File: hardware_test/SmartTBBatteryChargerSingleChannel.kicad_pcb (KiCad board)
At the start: 2 copper layers, 100 x 100 mm, 151 parts, among them J1 XT60_MALE, J2 XT60_MALE, J3 XT60_MALE, J7 Conn_SWD, J8 Conn_01x02, Q1 BSC070N10NS5, Q2 BSC070N10NS5, Q3 BSC070N10NS5, U1 RY8411, U10 INA240A1PW, U2 RS3236, U3 RY8411, U4 STM32G474RBTx, U5 INA240A1PW, U6 UCC27517, U7 UCC27517, U8 INA240A1PW, U9 UCC27517, Y1 Crystal_GND24

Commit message: Test Hardware schematic done
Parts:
- removed C51, C52, C61: 100u, Capacitor_THT:CP_Radial_D6.3mm_P2.50mm
- removed C53, C56, C57, C58, C60: 100n, Capacitor_SMD:C_0603_1608Metric
- removed C54, C55, C59: 10u, Capacitor_SMD:C_1206_3216Metric
- removed D16: LED_RED, LED_SMD:LED_0603_1608Metric
- removed D7: K34, Diode_SMD:D_SOD-123F
- removed D8: SB1045, Diode_SMD:D_PowerDI-5
- removed F3: 8A, Fuse:Fuse_1206_3216Metric
- removed J3: XT60_MALE, Connector_AMASS:AMASS_XT60-M_1x02_P7.20mm_Vertical
- removed L5: 47u, Inductor_SMD:L_Coilcraft_MSS1260-XXX
- removed Q3: BSC070N10NS5, Package_TO_SOT_SMD:TDSON-8-1
- removed R18: 10k, Resistor_SMD:R_0603_1608Metric
- removed R19: 90k, Resistor_SMD:R_0603_1608Metric
- removed R20: 4m, Resistor_SMD:R_Shunt_Vishay_WSK2512_6332Metric_T1.19mm
- removed R38: 240k, Resistor_SMD:R_0603_1608Metric
- removed U10: INA240A1PW, Package_SO:TSSOP-8_4.4x3mm_P0.65mm
- removed U9: UCC27517, Package_TO_SOT_SMD:SOT-23-5
- C21: value 100u 6.3V -> C_Polarized; footprint Capacitor_SMD:C_1206_3216Metric -> Capacitor_THT:CP_Radial_D6.3mm_P2.50mm
- C41: value 100u -> 100n; footprint Capacitor_THT:CP_Radial_D6.3mm_P2.50mm -> Capacitor_SMD:C_0603_1608Metric; moved to B.Cu
- C42: value 100n -> 100u; footprint Capacitor_SMD:C_0603_1608Metric -> Capacitor_THT:CP_Radial_D6.3mm_P2.50mm; moved to F.Cu
- C43: value 10u -> 100n; footprint Capacitor_SMD:C_1206_3216Metric -> Capacitor_SMD:C_0603_1608Metric
- C44: value 10u -> 100n; footprint Capacitor_SMD:C_1206_3216Metric -> Capacitor_SMD:C_0603_1608Metric; moved to F.Cu
- C45: value 100n -> 10u; footprint Capacitor_SMD:C_0603_1608Metric -> Capacitor_SMD:C_1206_3216Metric
- C46: value 100n -> 10u; footprint Capacitor_SMD:C_0603_1608Metric -> Capacitor_SMD:C_1206_3216Metric; moved to B.Cu
- C47: value 100n -> 10u; footprint Capacitor_SMD:C_0603_1608Metric -> Capacitor_SMD:C_1206_3216Metric; moved to F.Cu
- C48: value 10u -> 100u; footprint Capacitor_SMD:C_1206_3216Metric -> Capacitor_THT:CP_Radial_D6.3mm_P2.50mm
- C49: moved to B.Cu
- C50: value 100u -> 100n; footprint Capacitor_THT:CP_Radial_D6.3mm_P2.50mm -> Capacitor_SMD:C_0603_1608Metric
- D5: value K34 -> SB1045; footprint Diode_SMD:D_SOD-123F -> Diode_SMD:D_PowerDI-5
- D6: value SB1045 -> K34; footprint Diode_SMD:D_PowerDI-5 -> Diode_SMD:D_SOD-123F
- R11: value 1R -> 33R; moved to F.Cu
- R12: value 33R -> 4m; footprint Resistor_SMD:R_0603_1608Metric -> Resistor_SMD:R_Shunt_Vishay_WSK2512_6332Metric_T1.19mm; moved to B.Cu
- R13: value 10k -> 1R; moved to B.Cu
- R14: value 90k -> 10k
- R15: value 4m -> 90k; footprint Resistor_SMD:R_Shunt_Vishay_WSK2512_6332Metric_T1.19mm -> Resistor_SMD:R_0603_1608Metric; moved to F.Cu
- R16: value 1R -> 33r; moved to F.Cu
- R17: value 33R -> 33r
- U7: value UCC27517 -> INA240A1PW; footprint Package_TO_SOT_SMD:SOT-23-5 -> Package_SO:TSSOP-8_4.4x3mm_P0.65mm
- U8: value INA240A1PW -> UCC27517; footprint Package_SO:TSSOP-8_4.4x3mm_P0.65mm -> Package_TO_SOT_SMD:SOT-23-5
- moved R17 300.4 mm to (111.2, 155.0)
- moved R16 280.3 mm to (111.2, 152.5), turned to 0 degrees
- moved C44 34.4 mm to (400.4, 42.7), turned to 0 degrees
- moved C46 33.3 mm to (367.0, 51.0), turned to 180 degrees
- moved R13 24.7 mm to (381.2, 57.0), turned to -90 degrees
- moved C50 24.2 mm to (400.4, 45.2)
- moved R11 21.2 mm to (400.4, 47.7), turned to 0 degrees
- moved U7 20.9 mm to (369.8, 42.5)
- moved U8 20.5 mm to (384.2, 57.2)
- moved C45 20.0 mm to (365.8, 54.8), turned to -90 degrees
- moved R15 18.9 mm to (400.4, 52.8)
- moved R12 17.0 mm to (383.8, 43.0)
- moved C21 15.7 mm to (104.0, 155.2)
- moved C49 15.4 mm to (386.3, 54.5)
- moved C47 12.3 mm to (382.2, 44.0), turned to -90 degrees
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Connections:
- C41 pad 1: VPP -> +3.3V
- C44 pad 1: VPP -> GND
- C44 pad 2: GND -> ISENSE_CH2
- C45 pad 1: +10V -> VPP
- C46 pad 1: GND -> VPP
- C46 pad 2: ISENSE_CH2 -> GND
- C47 pad 1: +3.3V -> VPP
- C47 pad 2: GND -> Net-(C47-Pad2)
- C48 pad 2: Net-(C48-Pad2) -> Net-(C47-Pad2)
- C49 pad 1: GND -> +10V
- C49 pad 2: VSENSE_CH2 -> GND
- C50 pad 1: VPP -> GND
- C50 pad 2: Net-(C48-Pad2) -> VSENSE_CH2
- D5 pad 1: Net-(D5-K) -> VPP
- D6 pad 1: VPP -> Net-(D6-K)
- F2 pad 2: Net-(C48-Pad2) -> Net-(C47-Pad2)
- L4 pad 1: Net-(D6-A) -> Net-(D5-A)
- L4 pad 2: Net-(C48-Pad2) -> Net-(C47-Pad2)
- Q2 pad 4: Net-(D5-A) -> Net-(D6-A)
- Q2 pad 5: Net-(D6-A) -> Net-(D5-A)
- R11 pad 1: Net-(D5-K) -> ISENSE_CH2
- R11 pad 2: Net-(D5-A) -> Net-(R11-Pad2)
- R12 pad 1: ISENSE_CH2 -> VPP
- R12 pad 2: Net-(R12-Pad2) -> Net-(U7--)
- R13 pad 1: GND -> Net-(D6-K)
- R13 pad 2: VSENSE_CH2 -> Net-(D6-A)
- R14 pad 1: VSENSE_CH2 -> GND
- R14 pad 2: Net-(C48-Pad2) -> VSENSE_CH2
- R15 pad 1: VPP -> VSENSE_CH2
- R15 pad 2: Net-(U8--) -> Net-(C47-Pad2)
- R16 pad 1: Net-(D7-K) -> DRV_CH1
- R16 pad 2: Net-(D7-A) -> Net-(U4-PA8)
- R17 pad 1: ISENSE_CH3 -> DRV_CH2
- R17 pad 2: Net-(R17-Pad2) -> Net-(U4-PA10)
- U4 pad 15: Net-(U4-VSS-Pad15) -> GND
- U4 pad 27: unconnected-(U4-VSSA-Pad27) -> GND
- U4 pad 31: Net-(U4-VSS-Pad15) -> GND
- U4 pad 33: unconnected-(U4-PB11-Pad33) -> VSENSE_CH1
- U4 pad 35: unconnected-(U4-PB13-Pad35) -> VSENSE_CH2
- U4 pad 42: unconnected-(U4-PA8-Pad42) -> Net-(U4-PA8)
- U4 pad 44: unconnected-(U4-PA10-Pad44) -> Net-(U4-PA10)
- U4 pad 47: Net-(U4-VSS-Pad15) -> GND
- U4 pad 63: Net-(U4-VSS-Pad15) -> GND
- U4 pad 8: unconnected-(U4-PC0-Pad8) -> ISENSE_CH1
- U4 pad 9: unconnected-(U4-PC1-Pad9) -> ISENSE_CH2
- U7 pad 1: +10V -> GND
- U7 pad 2: GND -> Net-(U7-+)
- U7 pad 3: DRV_CH2 -> Net-(U7--)
- U7 pad 5: Net-(D5-K) -> +3.3V
- U8 pad 1: GND -> +10V
- U8 pad 2: Net-(U8-+) -> GND
- U8 pad 3: Net-(U8--) -> DRV_CH2
- U8 pad 5: +3.3V -> Net-(D6-K)

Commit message: Progress on hardware_test PCB
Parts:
- removed C24: 100n, Capacitor_SMD:C_0603_1608Metric
- removed Y1: Crystal_GND24, Crystal:Crystal_SMD_3225-4Pin_3.2x2.5mm
- added C51: 100n, Capacitor_SMD:C_0603_1608Metric, F.Cu at (227.1, 137.3)
- added C52: 100n, Capacitor_SMD:C_0603_1608Metric, F.Cu at (208.0, 131.6)
- added C53: 100n, Capacitor_SMD:C_0603_1608Metric, F.Cu at (208.0, 134.1)
- added C54: 10u, Capacitor_SMD:C_0603_1608Metric, F.Cu at (140.1, 103.3)
- added C55: 10u, Capacitor_SMD:C_0603_1608Metric, F.Cu at (140.1, 105.8)
- added C56: 20p, Capacitor_SMD:C_0603_1608Metric, F.Cu at (140.1, 108.3)
- added C57: 10u, Capacitor_SMD:C_0603_1608Metric, F.Cu at (345.5, 28.0)
- added D7: LED_WHITE, LED_SMD:LED_0603_1608Metric, F.Cu at (152.2, 103.7)
- added D8: LED_WHITE, LED_SMD:LED_0603_1608Metric, F.Cu at (152.2, 106.3)
- added D9: DSS34, Diode_SMD:D_SMF, F.Cu at (153.0, 100.7)
- added FB1: FerriteBead, Inductor_SMD:L_0603_1608Metric, F.Cu at (144.1, 98.2)
- added Q3: AO3400A, Package_TO_SOT_SMD:SOT-23, F.Cu at (152.6, 110.0)
- added R18: 1k, Resistor_SMD:R_0603_1608Metric, F.Cu at (81.6, 38.6)
- added R19: 100k, Resistor_SMD:R_0603_1608Metric, F.Cu at (144.1, 103.3)
- added R20: 10k, Resistor_SMD:R_0603_1608Metric, F.Cu at (144.1, 105.8)
- added R21: 2.2k, Resistor_SMD:R_0603_1608Metric, F.Cu at (144.1, 108.3)
- added R22: 33R, Resistor_SMD:R_0603_1608Metric, F.Cu at (208.0, 136.6)
- added R23: 4m, Resistor_SMD:R_Shunt_Vishay_WSK2512_6332Metric_T1.19mm, F.Cu at (225.0, 140.0)
- added R24: 10k, Resistor_SMD:R_0603_1608Metric, F.Cu at (208.0, 139.1)
- added R25: 90k, Resistor_SMD:R_0603_1608Metric, F.Cu at (208.0, 141.7)
- added R26: 33r, Resistor_SMD:R_0603_1608Metric, F.Cu at (148.1, 103.3)
- added R27: 10k, Resistor_SMD:R_0603_1608Metric, F.Cu at (148.1, 105.8)
- added U9: INA240A1PW, Package_SO:TSSOP-8_4.4x3mm_P0.65mm, F.Cu at (225.0, 135.0)
- added Y3: CSTCE8M, Crystal:Resonator_SMD_Murata_CSTxExxV-3Pin_3.0x1.1mm_HandSoldering, F.Cu at (349.5, 47.0)
- J8: footprint Connector_AMASS:AMASS_XT60PW-M_1x02_P7.20mm_Horizontal -> Connector_AMASS:AMASS_XT30U-M_1x02_P5.0mm_Vertical
- moved F7 315.2 mm to (354.0, 25.5)
- moved J7 309.0 mm to (357.5, 20.0), turned to 180 degrees
- moved C25 296.6 mm to (360.8, 33.5), turned to 180 degrees
- moved C23 292.4 mm to (356.5, 46.8), turned to 90 degrees
- moved C28 290.7 mm to (355.0, 46.8), turned to 90 degrees
- moved C91 290.1 mm to (360.8, 35.0), turned to 180 degrees
- moved C90 289.7 mm to (360.8, 36.5), turned to 180 degrees
- moved C26 283.1 mm to (347.0, 28.0), turned to -90 degrees
- moved C29 276.7 mm to (340.7, 39.5)
- moved C27 276.5 mm to (340.7, 41.0)
- moved R37 275.8 mm to (359.5, 26.0), turned to 90 degrees
- moved R36 274.2 mm to (358.0, 26.0), turned to 90 degrees
- moved R16 269.8 mm to (350.5, 28.0), turned to -90 degrees
- moved R17 269.6 mm to (349.0, 28.0), turned to -90 degrees
- moved F8 176.2 mm to (227.0, 143.5)
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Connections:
- C90 pad 2: Net-(U4-VREF+) -> +2V5
- C91 pad 2: Net-(U4-VREF+) -> +2V5
- D17 pad 1: unconnected-(D17-K-Pad1) -> GND
- D17 pad 2: unconnected-(D17-A-Pad2) -> Net-(D17-A)
- D18 pad 3: unconnected-(D18-DIN-Pad3) -> RGB_DATA
- F8 pad 1: VPP -> Net-(F8-Pad1)
- U4 pad 21: unconnected-(U4-PA7-Pad21) -> VSENSE_CH1
- U4 pad 24: BOOT0 -> VSENSE_CH2
- U4 pad 28: Net-(U4-VREF+) -> +2V5
- U4 pad 33: VSENSE_CH1 -> unconnected-(U4-PB11-Pad33)
- U4 pad 35: VSENSE_CH2 -> VSENSE_INPUT
- U4 pad 45: unconnected-(U4-PA11-Pad45) -> RGB_DATA
- U4 pad 54: unconnected-(U4-PC12-Pad54) -> BUZZER
- U4 pad 61: unconnected-(U4-PB8-Pad61) -> Net-(U4-PB8)
- U5 pad 6: +3.3V -> +2V5
- U7 pad 6: +3.3V -> +2V5

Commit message: just more wiring...
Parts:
- added BZ1: Buzzer-9032, LinkedLibrary:MLT-9032, F.Cu at (65.8, 77.7)
- C1, C10, C11, C12, C13, C14, C15, C16, C17, C18, C19, C2, C21, C3, C38, C44, C5, C51, C52, C6, C7, C8, C9, D1, D2, F8, L1, L2, R1, R10, R11, R14, R15, R19, R2, R20, R22, R23, R3, R4, R8, R9, U1, U2, U3, U9: moved to B.Cu
- moved C38 332.5 mm to (69.6, 61.5), turned to -90 degrees
- moved C44 329.8 mm to (71.1, 61.5), turned to -90 degrees
- moved C39 320.7 mm to (81.2, 61.9), turned to 180 degrees
- moved C50 319.5 mm to (81.3, 60.4), turned to 180 degrees
- moved R11 312.5 mm to (88.1, 59.7)
- moved R8 311.9 mm to (88.1, 38.6)
- moved R14 298.2 mm to (102.6, 66.0)
- moved R9 297.3 mm to (102.9, 44.9)
- moved R15 294.8 mm to (105.9, 66.0)
- moved R10 293.9 mm to (106.2, 44.9)
- moved C31 286.1 mm to (85.9, 42.9), turned to -90 degrees
- moved C41 286.1 mm to (85.6, 64.3), turned to -90 degrees
- moved C49 281.6 mm to (105.4, 74.4)
- moved C23 281.2 mm to (76.1, 68.0), turned to -90 degrees
- moved C22 281.0 mm to (105.7, 53.5)
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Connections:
- U4 pad 10: unconnected-(U4-PC2-Pad10) -> ISENSE_INPUT
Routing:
- net DRV_CH2: track 0.00 -> 68.8 mm, vias 0 -> 1
- net VSENSE_CH1: track 0.00 -> 49.3 mm, vias 0 -> 3
- net DRV_CH1: track 0.00 -> 44.3 mm, vias 0 -> 1
- net RGB_DATA: track 0.00 -> 43.6 mm
- net ISENSE_CH1: track 0.00 -> 42.8 mm, vias 0 -> 2
- net VSENSE_CH2: track 0.00 -> 42.1 mm, vias 0 -> 1
- net +3.3V: track 0.00 -> 42.1 mm, vias 0 -> 4
- net +2V5: track 0.38 -> 41.1 mm, vias 0 -> 4
- net +10V: track 0.00 -> 32.5 mm, vias 0 -> 10
- net Net-(D19-DOUT): track 0.00 -> 31.9 mm
- net +5V: track 0.00 -> 28.4 mm
- net Net-(C36-Pad2): track 0.00 -> 25.0 mm, vias 0 -> 2
- net SWDIO: track 0.00 -> 24.8 mm
- net SWDCK: track 0.00 -> 24.5 mm
- net Net-(C47-Pad2): track 0.00 -> 23.5 mm, vias 0 -> 2
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- added copper zone on In2.Cu, net +10V
- added copper zone on In1.Cu, net GND
- added copper zone on In2.Cu, net VPP
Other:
- board size 100 x 100 mm -> 69.2 x 49.9 mm
- copper layers 2 -> 4

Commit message: Revert "just more wiring..."
This reverts commit 3ec1996944e63c1d6ae5bd01b13986183c75ca17.
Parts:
- removed BZ1: Buzzer-9032, LinkedLibrary:MLT-9032
- C1, C10, C11, C12, C13, C14, C15, C16, C17, C18, C19, C2, C21, C3, C38, C44, C5, C51, C52, C6, C7, C8, C9, D1, D2, F8, L1, L2, R1, R10, R11, R14, R15, R19, R2, R20, R22, R23, R3, R4, R8, R9, U1, U2, U3, U9: moved to F.Cu
- moved C38 332.5 mm to (399.8, 22.5), turned to 180 degrees
- moved C44 329.8 mm to (400.4, 42.7), turned to 0 degrees
- moved C39 320.7 mm to (399.8, 25.0), turned to 0 degrees
- moved C50 319.5 mm to (400.4, 45.2), turned to 0 degrees
- moved R11 312.5 mm to (400.4, 47.7)
- moved R8 311.9 mm to (399.8, 27.5)
- moved R14 298.2 mm to (400.4, 50.2)
- moved R9 297.3 mm to (399.8, 30.0)
- moved R15 294.8 mm to (400.4, 52.8)
- moved R10 293.9 mm to (399.8, 32.5)
- moved C31 286.1 mm to (371.3, 24.0), turned to 0 degrees
- moved C41 286.1 mm to (371.0, 45.0), turned to 180 degrees
- moved C49 281.6 mm to (386.3, 54.5)
- moved C23 281.2 mm to (356.5, 46.8), turned to 90 degrees
- moved C22 281.0 mm to (386.0, 33.5)
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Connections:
- U4 pad 10: ISENSE_INPUT -> unconnected-(U4-PC2-Pad10)
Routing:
- net DRV_CH2: track 68.8 -> 0.00 mm, vias 1 -> 0
- net VSENSE_CH1: track 49.3 -> 0.00 mm, vias 3 -> 0
- net DRV_CH1: track 44.3 -> 0.00 mm, vias 1 -> 0
- net RGB_DATA: track 43.6 -> 0.00 mm
- net ISENSE_CH1: track 42.8 -> 0.00 mm, vias 2 -> 0
- net VSENSE_CH2: track 42.1 -> 0.00 mm, vias 1 -> 0
- net +3.3V: track 42.1 -> 0.00 mm, vias 4 -> 0
- net +2V5: track 41.1 -> 0.38 mm, vias 4 -> 0
- net +10V: track 32.5 -> 0.00 mm, vias 10 -> 0
- net Net-(D19-DOUT): track 31.9 -> 0.00 mm
- net +5V: track 28.4 -> 0.00 mm
- net Net-(C36-Pad2): track 25.0 -> 0.00 mm, vias 2 -> 0
- net SWDIO: track 24.8 -> 0.00 mm
- net SWDCK: track 24.5 -> 0.00 mm
- net Net-(C47-Pad2): track 23.5 -> 0.00 mm, vias 2 -> 0
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- removed copper zone on In2.Cu, net +10V
- removed copper zone on In1.Cu, net GND
- removed copper zone on In2.Cu, net VPP
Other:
- board size 69.2 x 49.9 mm -> 100 x 100 mm
- copper layers 4 -> 2

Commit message: feat(hardware_test): Signal wire, VPP/+3.3V (@power plane) finished layout
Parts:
- added BZ1: Buzzer-9032, LinkedLibrary:MLT-9032, F.Cu at (65.8, 77.7)
- C1, C10, C11, C12, C13, C14, C15, C16, C17, C18, C19, C2, C3, C38, C44, C5, C51, C52, C6, C7, C8, C9, D1, D2, F8, L1, L2, R1, R10, R11, R14, R15, R19, R2, R20, R22, R23, R3, R4, R8, R9, U1, U2, U3, U9: moved to B.Cu
- moved C38 332.5 mm to (69.6, 61.5), turned to -90 degrees
- moved C44 329.8 mm to (71.1, 61.5), turned to -90 degrees
- moved C39 320.7 mm to (81.2, 61.9), turned to 180 degrees
- moved C50 319.5 mm to (81.3, 60.4), turned to 180 degrees
- moved R11 312.5 mm to (88.1, 59.7)
- moved R8 311.9 mm to (88.1, 38.6)
- moved R14 298.2 mm to (102.6, 66.0)
- moved R9 297.3 mm to (102.9, 44.9)
- moved R15 294.8 mm to (105.9, 66.0)
- moved R10 293.9 mm to (106.2, 44.9)
- moved C28 290.2 mm to (65.5, 67.3)
- moved C31 286.1 mm to (85.9, 42.9), turned to -90 degrees
- moved C41 286.1 mm to (85.6, 64.3), turned to -90 degrees
- moved C57 284.6 mm to (63.2, 64.8), turned to 0 degrees
- moved C49 281.6 mm to (105.4, 74.4)
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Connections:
- U4 pad 10: unconnected-(U4-PC2-Pad10) -> ISENSE_INPUT
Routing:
- net DRV_CH2: track 0.00 -> 68.8 mm, vias 0 -> 1
- net +3.3V: track 0.00 -> 64.4 mm, vias 0 -> 26
- net +5V: track 0.00 -> 54.3 mm, vias 0 -> 13
- net VSENSE_CH1: track 0.00 -> 50.2 mm, vias 0 -> 3
- net DRV_CH1: track 0.00 -> 44.3 mm, vias 0 -> 1
- net RGB_DATA: track 0.00 -> 43.6 mm
- net ISENSE_CH1: track 0.00 -> 42.1 mm, vias 0 -> 2
- net VSENSE_CH2: track 0.00 -> 42.0 mm, vias 0 -> 1
- net Net-(D19-DOUT): track 0.00 -> 32.0 mm
- net VPP: track 17.4 -> 46.7 mm, vias 0 -> 18
- net +10V: track 0.00 -> 28.7 mm, vias 0 -> 10
- net Net-(C36-Pad2): track 0.00 -> 25.0 mm, vias 0 -> 2
- net SWDIO: track 0.00 -> 24.8 mm
- net SWDCK: track 0.00 -> 24.5 mm
- net Net-(C47-Pad2): track 0.00 -> 23.5 mm, vias 0 -> 2
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- added copper zone on In2.Cu, net +10V
- added copper zone on In2.Cu, net +3.3V
- added copper zone on In2.Cu, net +5V
- added copper zone on In1.Cu, net GND
- added copper zone on In2.Cu, net VPP
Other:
- board size 100 x 100 mm -> 69.2 x 49.9 mm
- copper layers 2 -> 4

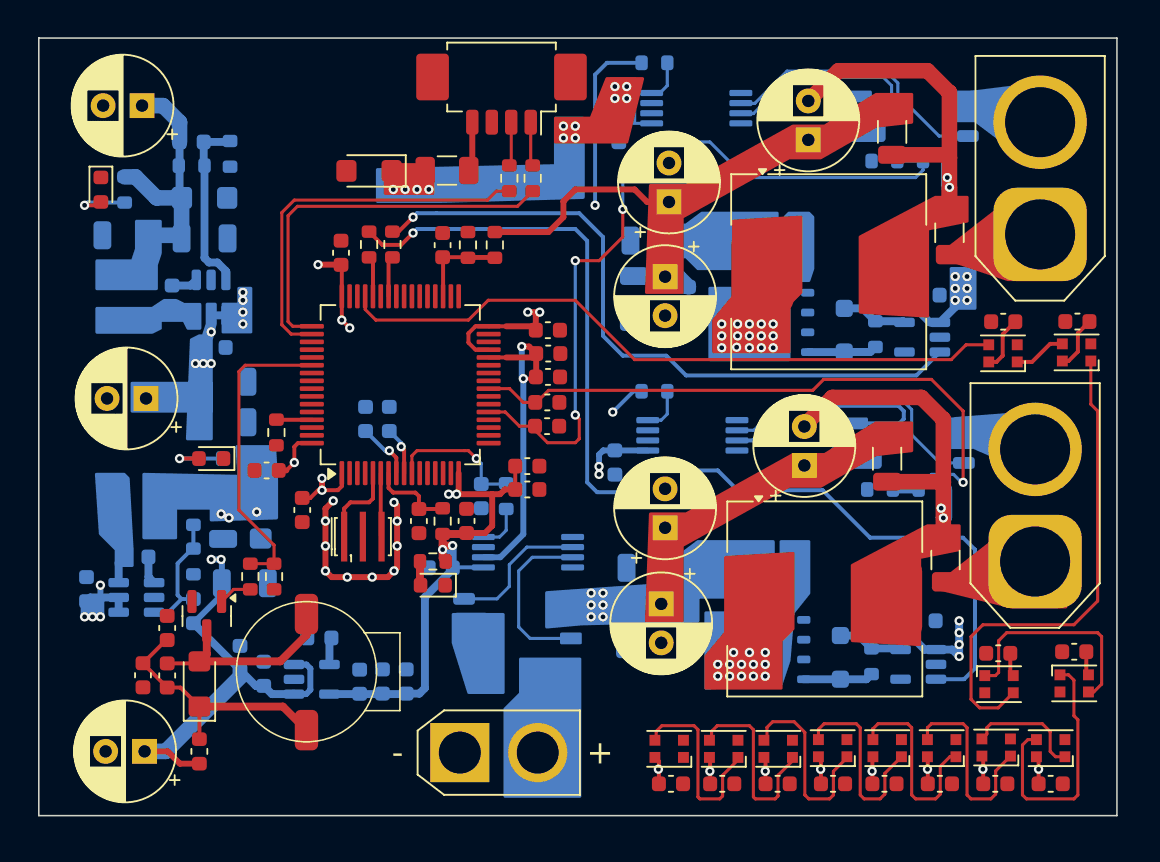
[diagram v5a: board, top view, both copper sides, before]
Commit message: feat(SmartTBBatteryChargerSingleChannel.kicad_pcb): Power plane layout finished
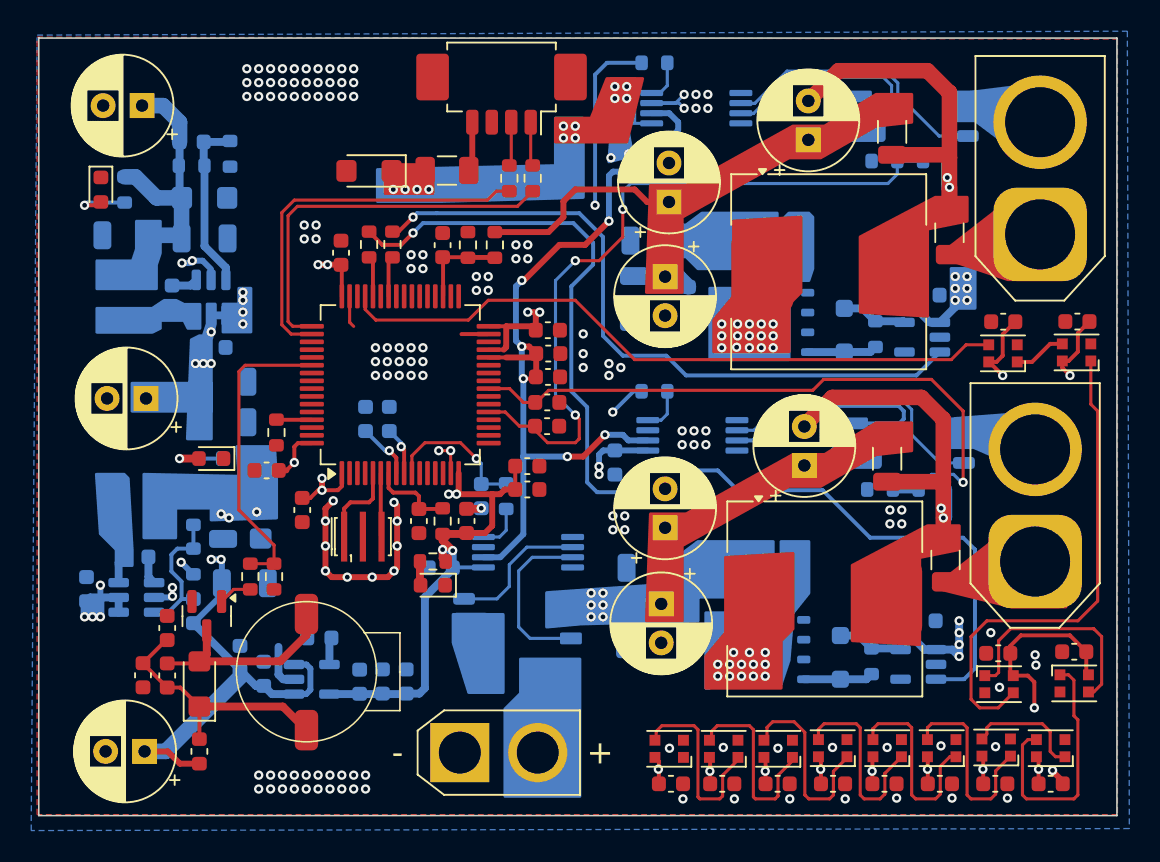
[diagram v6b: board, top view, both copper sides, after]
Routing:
- net +2V5: track 21.9 -> 54.3 mm, vias 2 -> 6
- net GND: track 14.0 -> 35.3 mm, vias 10 -> 146
- net +5V: track 54.3 -> 65.9 mm, vias 13 -> 16
- net +3.3V: track 64.4 -> 60.7 mm, vias 26 -> 25
- net VSENSE_CH1: track 50.2 -> 46.6 mm
- net DRV_CH2: track 68.8 -> 70.5 mm
- net Net-(U1-FB): track 8.20 -> 9.10 mm
- added copper zone on B.Cu, net GND
- added copper zone on F.Cu, net GND

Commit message: fix(SmartTBBatteryChargerSingleChannel.kicad_pcb): Finished route
BREAKING CHANGE:
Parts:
- moved R4 4.12 mm to (58.6, 74.7)
- moved C5 2.67 mm to (61.2, 79.5), turned to -90 degrees
- moved C15 2.17 mm to (58.6, 71.6), turned to -90 degrees
- moved C3 1.66 mm to (62.7, 79.5), turned to -90 degrees
- moved C7 0.81 mm to (51.2, 73.0)
- moved U1 0.69 mm to (54.2, 72.8)
- moved D3 0.24 mm to (94.6, 49.8)
- moved C43 0.17 mm to (90.4, 74.9)
- moved C22 0.13 mm to (105.6, 53.6), turned to 180 degrees
- moved Q2 0.12 mm to (94.9, 76.3)
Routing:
- net GND: track 35.3 -> 27.1 mm, vias 146 -> 145
- net +5V: track 65.9 -> 59.2 mm
- net VPP: track 46.7 -> 41.9 mm, vias 18 -> 17
- net Net-(U1-FB): track 9.10 -> 10.2 mm
- net Net-(U1-LX): track 1.80 -> 2.79 mm
- net +10V: track 28.7 -> 28.1 mm
- net Net-(U1-BS): track 1.80 -> 1.29 mm
